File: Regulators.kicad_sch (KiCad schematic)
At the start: 20 parts, among them IC1 LT8631IFE#PBF, J10 1935161

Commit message: progress
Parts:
- C53: renamed from C1; footprint CAPAE1360X1450N -> SamacSys_Parts:CAPAE1360X1450N
- renumbered C13 to C54, C16 to C55, C18 to C56, C20 to C57, C21 to C58, C23 to C59, C17 to C60, D22 to D24, D3 to D25, IC1 to IC2, J10 to J18, R91 to R90, R108 to R91, R44 to R92, R45 to R93, R46 to R94, R47 to R95, R48 to R96
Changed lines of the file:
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@@
 		(dnp no)
 		(fields_autoplaced yes)
-		(property "Reference" "C13"
+		(property "Reference" "C54"
 			(at 139.7 44.4499 0)
 			(show_name no)
@@
 			(project "kiln"
 				(path "/e9c1836b-d16f-494a-819b-41549a786e18/415569b5-e71f-44a8-96ab-1860fbe1fd72"
-					(reference "C15")
+					(reference "C62")
 					(unit 1)
 				)
 				(path "/e9c1836b-d16f-494a-819b-41549a786e18/79a7153e-7b60-438c-928b-888b0e0879ef"
-					(reference "C13")
+					(reference "C54")
 					(unit 1)
 				)
@@
 		(dnp no)
 		(fields_autoplaced yes)
-		(property "Reference" "R91"
+		(property "Reference" "R90"
 			(at 123.19 76.1999 0)
 			(show_name no)
@@
 			(project "kiln"
 				(path "/e9c1836b-d16f-494a-819b-41549a786e18/415569b5-e71f-44a8-96ab-1860fbe1fd72"
-					(reference "R107")
+					(reference "R97")
 					(unit 1)
 				)
 				(path "/e9c1836b-d16f-494a-819b-41549a786e18/79a7153e-7b60-438c-928b-888b0e0879ef"
-					(reference "R91")
+					(reference "R90")
 					(unit 1)
 				)
@@
 		(dnp no)
 		(fields_autoplaced yes)
-		(property "Reference" "R47"
+		(property "Reference" "R95"
 			(at 236.22 81.2799 0)
 			(show_name no)
@@
 			(project "kiln"
 				(path "/e9c1836b-d16f-494a-819b-41549a786e18/415569b5-e71f-44a8-96ab-1860fbe1fd72"
-					(reference "R87")
+					(reference "R102")
 					(unit 1)
 				)
 				(path "/e9c1836b-d16f-494a-819b-41549a786e18/79a7153e-7b60-438c-928b-888b0e0879ef"
-					(reference "R47")
+					(reference "R95")
 					(unit 1)
 				)
@@
 		(in_pos_files yes)
 		(dnp no)
-		(property "Reference" "C18"
+		(property "Reference" "C56"
 			(at 202.438 85.344 0)
 			(show_name no)
@@
 			(project "kiln"
 				(path "/e9c1836b-d16f-494a-819b-41549a786e18/415569b5-e71f-44a8-96ab-1860fbe1fd72"
-					(reference "C45")
+					(reference "C64")
 					(unit 1)
 				)
 				(path "/e9c1836b-d16f-494a-819b-41549a786e18/79a7153e-7b60-438c-928b-888b0e0879ef"
-					(reference "C18")
+					(reference "C56")
 					(unit 1)
 				)
@@
 		(dnp no)
 		(fields_autoplaced yes)
-		(property "Reference" "C17"
+		(property "Reference" "C60"
 			(at 266.7 85.0899 0)
 			(show_name no)
@@
 			(project "kiln"
 				(path "/e9c1836b-d16f-494a-819b-41549a786e18/415569b5-e71f-44a8-96ab-1860fbe1fd72"
-					(reference "C49")
+					(reference "C68")
 					(unit 1)
 				)
 				(path "/e9c1836b-d16f-494a-819b-41549a786e18/79a7153e-7b60-438c-928b-888b0e0879ef"
-					(reference "C17")
+					(reference "C60")
 					(unit 1)
 				)
@@
 		(dnp no)
 		(fields_autoplaced yes)
-		(property "Reference" "C21"
+		(property "Reference" "C58"
 			(at 224.79 80.0099 0)
 			(show_name no)
@@
 			(project "kiln"
 				(path "/e9c1836b-d16f-494a-819b-41549a786e18/415569b5-e71f-44a8-96ab-1860fbe1fd72"
-					(reference "C47")
+					(reference "C66")
 					(unit 1)
 				)
 				(path "/e9c1836b-d16f-494a-819b-41549a786e18/79a7153e-7b60-438c-928b-888b0e0879ef"
-					(reference "C21")
+					(reference "C58")
 					(unit 1)
 				)
@@
 		(dnp no)
 		(fields_autoplaced yes)
-		(property "Reference" "D3"
+		(property "Reference" "D25"
 			(at 124.46 96.8374 90)
 			(show_name no)
@@
 			(project "kiln"
 				(path "/e9c1836b-d16f-494a-819b-41549a786e18/415569b5-e71f-44a8-96ab-1860fbe1fd72"
-					(reference "D4")
+					(reference "D27")
 					(unit 1)
 				)
 				(path "/e9c1836b-d16f-494a-819b-41549a786e18/79a7153e-7b60-438c-928b-888b0e0879ef"
-					(reference "D3")
+					(reference "D25")
 					(unit 1)
 				)
@@
 			(project "kiln"
 				(path "/e9c1836b-d16f-494a-819b-41549a786e18/415569b5-e71f-44a8-96ab-1860fbe1fd72"
-					(reference "L5")
+					(reference "L3")
 					(unit 1)
 				)
@@
 		(dnp no)
 		(fields_autoplaced yes)
-		(property "Reference" "IC1"
+		(property "Reference" "IC2"
 			(at 184.15 48.26 0)
 			(show_name no)
@@
 			(project "kiln"
 				(path "/e9c1836b-d16f-494a-819b-41549a786e18/415569b5-e71f-44a8-96ab-1860fbe1fd72"
+					(reference "IC3")
+					(unit 1)
+				)
+				(path "/e9c1836b-d16f-494a-819b-41549a786e18/79a7153e-7b60-438c-928b-888b0e0879ef"
 					(reference "IC2")
-					(unit 1)
-				)
-				(path "/e9c1836b-d16f-494a-819b-41549a786e18/79a7153e-7b60-438c-928b-888b0e0879ef"
-					(reference "IC1")
 					(unit 1)
 				)
@@
 		(dnp no)
 		(fields_autoplaced yes)
-		(property "Reference" "R108"
+		(property "Reference" "R91"
 			(at 123.19 85.0899 0)
 			(show_name no)
@@
 			(project "kiln"
 				(path "/e9c1836b-d16f-494a-819b-41549a786e18/415569b5-e71f-44a8-96ab-1860fbe1fd72"
-					(reference "R109")
+					(reference "R98")
 					(unit 1)
 				)
 				(path "/e9c1836b-d16f-494a-819b-41549a786e18/79a7153e-7b60-438c-928b-888b0e0879ef"
-					(reference "R108")
+					(reference "R91")
 					(unit 1)
 				)
@@
 		(dnp no)
 		(fields_autoplaced yes)
-		(property "Reference" "C16"
+		(property "Reference" "C55"
 			(at 163.83 88.8999 0)
 			(show_name no)
@@
 			(project "kiln"
 				(path "/e9c1836b-d16f-494a-819b-41549a786e18/415569b5-e71f-44a8-96ab-1860fbe1fd72"
-					(reference "C19")
+					(reference "C63")
 					(unit 1)
 				)
 				(path "/e9c1836b-d16f-494a-819b-41549a786e18/79a7153e-7b60-438c-928b-888b0e0879ef"
-					(reference "C16")
+					(reference "C55")
 					(unit 1)
 				)
@@
 		(dnp no)
 		(fields_autoplaced yes)
-		(property "Reference" "C1"
+		(property "Reference" "C53"
 			(at 124.46 45.7199 90)
 			(show_name no)
@@
 			)
 		)
-		(property "Footprint" "CAPAE1360X1450N"
+		(property "Footprint" "SamacSys_Parts:CAPAE1360X1450N"
 			(at 121.92 49.53 0)
 			(hide yes)
@@
 			(project "kiln"
 				(path "/e9c1836b-d16f-494a-819b-41549a786e18/415569b5-e71f-44a8-96ab-1860fbe1fd72"
-					(reference "C2")
+					(reference "C61")
 					(unit 1)
 				)
 				(path "/e9c1836b-d16f-494a-819b-41549a786e18/79a7153e-7b60-438c-928b-888b0e0879ef"
-					(reference "C1")
+					(reference "C53")
 					(unit 1)
 				)
@@
 		(dnp no)
 		(fields_autoplaced yes)
-		(property "Reference" "R46"
+		(property "Reference" "R94"
 			(at 152.4 83.8199 0)
 			(show_name no)
@@
 			(project "kiln"
 				(path "/e9c1836b-d16f-494a-819b-41549a786e18/415569b5-e71f-44a8-96ab-1860fbe1fd72"
-					(reference "R81")
+					(reference "R101")
 					(unit 1)
 				)
 				(path "/e9c1836b-d16f-494a-819b-41549a786e18/79a7153e-7b60-438c-928b-888b0e0879ef"
-					(reference "R46")
+					(reference "R94")
 					(unit 1)
 				)
@@
 		(in_pos_files yes)
 		(dnp no)
-		(property "Reference" "J10"
+		(property "Reference" "J18"
 			(at 90.17 35.56 0)
 			(show_name no)
@@
 				)
 				(path "/e9c1836b-d16f-494a-819b-41549a786e18/79a7153e-7b60-438c-928b-888b0e0879ef"
-					(reference "J10")
+					(reference "J18")
 					(unit 1)
 				)
@@
 		(dnp no)
 		(fields_autoplaced yes)
-		(property "Reference" "R45"
+		(property "Reference" "R93"
 			(at 149.86 54.6099 0)
 			(show_name no)
@@
 			(project "kiln"
 				(path "/e9c1836b-d16f-494a-819b-41549a786e18/415569b5-e71f-44a8-96ab-1860fbe1fd72"
-					(reference "R80")
+					(reference "R100")
 					(unit 1)
 				)
 				(path "/e9c1836b-d16f-494a-819b-41549a786e18/79a7153e-7b60-438c-928b-888b0e0879ef"
-					(reference "R45")
+					(reference "R93")
 					(unit 1)
 				)
@@
 		(in_pos_files yes)
 		(dnp no)
-		(property "Reference" "C23"
+		(property "Reference" "C59"
 			(at 246.634 86.868 90)
 			(show_name no)
@@
 			(project "kiln"
 				(path "/e9c1836b-d16f-494a-819b-41549a786e18/415569b5-e71f-44a8-96ab-1860fbe1fd72"
-					(reference "C48")
+					(reference "C67")
 					(unit 1)
 				)
 				(path "/e9c1836b-d16f-494a-819b-41549a786e18/79a7153e-7b60-438c-928b-888b0e0879ef"
-					(reference "C23")
+					(reference "C59")
 					(unit 1)
 				)
@@
 		(dnp no)
 		(fields_autoplaced yes)
-		(property "Reference" "R48"
+		(property "Reference" "R96"
 			(at 236.22 91.4399 0)
 			(show_name no)
@@
 			(project "kiln"
 				(path "/e9c1836b-d16f-494a-819b-41549a786e18/415569b5-e71f-44a8-96ab-1860fbe1fd72"
-					(reference "R88")
+					(reference "R103")
 					(unit 1)
 				)
 				(path "/e9c1836b-d16f-494a-819b-41549a786e18/79a7153e-7b60-438c-928b-888b0e0879ef"
-					(reference "R48")
+					(reference "R96")
 					(unit 1)
 				)
@@
 		(in_pos_files yes)
 		(dnp no)
-		(property "Reference" "D22"
+		(property "Reference" "D24"
 			(at 107.696 44.958 90)
 			(show_name no)
@@
 			(project "kiln"
 				(path "/e9c1836b-d16f-494a-819b-41549a786e18/415569b5-e71f-44a8-96ab-1860fbe1fd72"
-					(reference "D35")
+					(reference "D26")
 					(unit 1)
 				)
 				(path "/e9c1836b-d16f-494a-819b-41549a786e18/79a7153e-7b60-438c-928b-888b0e0879ef"
-					(reference "D22")
+					(reference "D24")
 					(unit 1)
 				)
@@
 		(dnp no)
 		(fields_autoplaced yes)
-		(property "Reference" "R44"
+		(property "Reference" "R92"
 			(at 149.86 44.4499 0)
 			(show_name no)
@@
 			(project "kiln"
 				(path "/e9c1836b-d16f-494a-819b-41549a786e18/415569b5-e71f-44a8-96ab-1860fbe1fd72"
-					(reference "R79")
+					(reference "R99")
 					(unit 1)
 				)
 				(path "/e9c1836b-d16f-494a-819b-41549a786e18/79a7153e-7b60-438c-928b-888b0e0879ef"
-					(reference "R44")
+					(reference "R92")
 					(unit 1)
 				)
@@
 		(dnp no)
 		(fields_autoplaced yes)
-		(property "Reference" "C20"
+		(property "Reference" "C57"
 			(at 220.98 54.6099 0)
 			(show_name no)
@@
 			(project "kiln"
 				(path "/e9c1836b-d16f-494a-819b-41549a786e18/415569b5-e71f-44a8-96ab-1860fbe1fd72"
-					(reference "C46")
+					(reference "C65")
 					(unit 1)
 				)
 				(path "/e9c1836b-d16f-494a-819b-41549a786e18/79a7153e-7b60-438c-928b-888b0e0879ef"
-					(reference "C20")
-					(unit 1)
-				)
+					(reference "C57")
+					(unit 1)
+				)

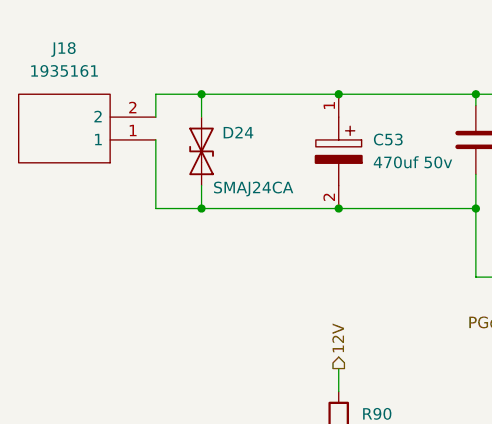
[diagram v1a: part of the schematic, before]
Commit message: why does c12 have a diffrent footprint from c67 and c56
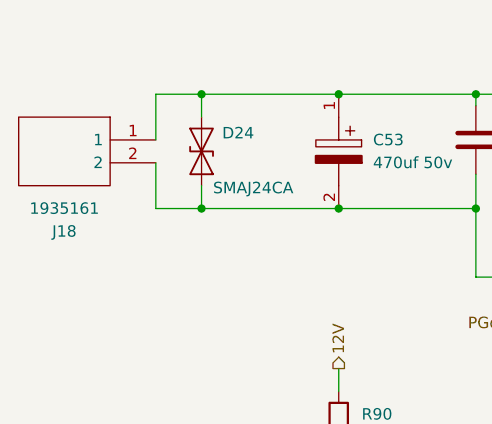
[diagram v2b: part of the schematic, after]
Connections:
- net 12V: now also J18.1; no longer J18.2
- net PwrGnd: now also J18.2; no longer J18.1
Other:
- moved on the sheet: J18
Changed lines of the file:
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@@
+	)
+	(junction
+		(at 243.84 97.79)
+		(diameter 0)
+		(color 0 0 0 0)
+	)
+	(junction
+		(at 233.68 76.2)
+		(diameter 0)
+		(color 0 0 0 0)
+	)
+	(junction
+		(at 144.78 40.64)
+		(diameter 0)
+		(color 0 0 0 0)
+	)
+	(junction
+		(at 147.32 40.64)
+		(diameter 0)
+		(color 0 0 0 0)
+	)
+	(junction
+		(at 120.65 40.64)
+		(diameter 0)
+		(color 0 0 0 0)
+	)
+	(junction
+		(at 250.19 97.79)
+		(diameter 0)
+		(color 0 0 0 0)
+	)
+	(junction
+		(at 233.68 97.79)
+		(diameter 0)
+		(color 0 0 0 0)
+	)
+	(junction
+		(at 147.32 60.96)
+		(diameter 0)
+		(color 0 0 0 0)
+	)
+	(junction
+		(at 120.65 53.34)
+		(diameter 0)
+		(color 0 0 0 0)
+	)
+	(junction
+		(at 105.41 53.34)
+		(diameter 0)
+		(color 0 0 0 0)
+	)
+	(junction
+		(at 160.02 97.79)
+		(diameter 0)
+		(color 0 0 0 0)
+	)
+	(junction
+		(at 135.89 53.34)
+		(diameter 0)
+		(color 0 0 0 0)
+	)
+	(junction
+		(at 147.32 76.2)
+		(diameter 0)
+		(color 0 0 0 0)
+	)
+	(junction
+		(at 250.19 76.2)
+		(diameter 0)
+		(color 0 0 0 0)
+	)
+	(junction
+		(at 220.98 87.63)
+		(diameter 0)
+		(color 0 0 0 0)
+	)
+	(junction
+		(at 233.68 87.63)
+		(diameter 0)
+		(color 0 0 0 0)
+	)
+	(junction
+		(at 213.36 97.79)
+		(diameter 0)
+		(color 0 0 0 0)
+	)
+	(junction
+		(at 135.89 40.64)
+		(diameter 0)
+		(color 0 0 0 0)
 	)
 	(junction
@@
 	)
 	(junction
-		(at 243.84 97.79)
-		(diameter 0)
-		(color 0 0 0 0)
-	)
-	(junction
-		(at 233.68 76.2)
-		(diameter 0)
-		(color 0 0 0 0)
-	)
-	(junction
-		(at 144.78 40.64)
-		(diameter 0)
-		(color 0 0 0 0)
-	)
-	(junction
-		(at 147.32 40.64)
-		(diameter 0)
-		(color 0 0 0 0)
-	)
-	(junction
-		(at 120.65 40.64)
-		(diameter 0)
-		(color 0 0 0 0)
-	)
-	(junction
-		(at 250.19 97.79)
-		(diameter 0)
-		(color 0 0 0 0)
-	)
-	(junction
-		(at 233.68 97.79)
-		(diameter 0)
-		(color 0 0 0 0)
-	)
-	(junction
-		(at 147.32 60.96)
-		(diameter 0)
-		(color 0 0 0 0)
-	)
-	(junction
-		(at 120.65 53.34)
-		(diameter 0)
-		(color 0 0 0 0)
-	)
-	(junction
-		(at 105.41 53.34)
-		(diameter 0)
-		(color 0 0 0 0)
-	)
-	(junction
-		(at 160.02 97.79)
-		(diameter 0)
-		(color 0 0 0 0)
-	)
-	(junction
-		(at 135.89 53.34)
-		(diameter 0)
-		(color 0 0 0 0)
-	)
-	(junction
-		(at 147.32 76.2)
-		(diameter 0)
-		(color 0 0 0 0)
-	)
-	(junction
-		(at 250.19 76.2)
-		(diameter 0)
-		(color 0 0 0 0)
-	)
-	(junction
-		(at 220.98 87.63)
-		(diameter 0)
-		(color 0 0 0 0)
-	)
-	(junction
-		(at 233.68 87.63)
-		(diameter 0)
-		(color 0 0 0 0)
-	)
-	(junction
-		(at 213.36 97.79)
-		(diameter 0)
-		(color 0 0 0 0)
-	)
-	(junction
-		(at 135.89 40.64)
-		(diameter 0)
-		(color 0 0 0 0)
-	)
-	(junction
 		(at 147.32 50.8)
 		(diameter 0)
@@
 	(wire
 		(pts
+			(xy 100.33 40.64) (xy 105.41 40.64)
+		)
+		(stroke
+			(width 0)
+			(type default)
+		)
+	)
+	(wire
+		(pts
 			(xy 207.01 83.82) (xy 207.01 66.04)
 		)
@@
 	(wire
 		(pts
-			(xy 100.33 40.64) (xy 105.41 40.64)
-		)
-		(stroke
-			(width 0)
-			(type default)
-		)
-	)
-	(wire
-		(pts
 			(xy 144.78 38.1) (xy 144.78 40.64)
 		)
@@
 	(wire
 		(pts
-			(xy 100.33 53.34) (xy 100.33 45.72)
-		)
-		(stroke
-			(width 0)
-			(type default)
-		)
-	)
-	(wire
-		(pts
 			(xy 204.47 60.96) (xy 217.17 60.96)
 		)
@@
 	(wire
 		(pts
+			(xy 100.33 45.72) (xy 100.33 40.64)
+		)
+		(stroke
+			(width 0)
+			(type default)
+		)
+	)
+	(wire
+		(pts
+			(xy 100.33 48.26) (xy 100.33 53.34)
+		)
+		(stroke
+			(width 0)
+			(type default)
+		)
+	)
+	(wire
+		(pts
 			(xy 207.01 91.44) (xy 207.01 97.79)
 		)
@@
 		(pts
 			(xy 233.68 71.12) (xy 204.47 71.12)
-		)
-		(stroke
-			(width 0)
-			(type default)
-		)
-	)
-	(wire
-		(pts
-			(xy 100.33 40.64) (xy 100.33 43.18)
 		)
 		(stroke
@@
 	(symbol
 		(lib_id "SamacSys_Parts:1935161")
-		(at 100.33 45.72 180)
+		(at 100.33 45.72 0)
+		(mirror y)
 		(unit 1)
 		(body_style 1)
@@
 		(dnp no)
 		(property "Reference" "J18"
-			(at 90.17 35.56 0)
+			(at 90.17 55.88 0)
 			(show_name no)
 			(do_not_autoplace no)
@@
 		)
 		(property "Value" "1935161"
-			(at 90.17 38.1 0)
+			(at 90.17 53.34 0)
 			(show_name no)
 			(do_not_autoplace no)
@@
 		)
 		(property "Footprint" "SamacSys_Parts:1935161"
-			(at 83.82 48.26 0)
+			(at 83.82 43.18 0)
 			(hide yes)
 			(show_name no)
@@
 		)
 		(property "Description_1" "Phoenix Contact COMBICON PT PCB Terminal Block, 2 Way/Pole, Screw Terminals, 26  14 AWG Through Hole, Nylon"
-			(at 83.82 43.18 0)
+			(at 83.82 48.26 0)
 			(hide yes)
 			(show_name no)
@@
 		)
 		(property "Height" "11.55"
-			(at 83.82 40.64 0)
+			(at 83.82 50.8 0)
 			(hide yes)
 			(show_name no)
@@
 		)
 		(property "Mouser Part Number" "651-1935161"
-			(at 83.82 38.1 0)
+			(at 83.82 53.34 0)
 			(hide yes)
 			(show_name no)
@@
 		)
 		(property "Mouser Price/Stock" "https://www.mouser.co.uk/ProductDetail/Phoenix-Contact/1935161?qs=W3wJikR1%252BS6eKzfFl8Rbew%3D%3D"
-			(at 83.82 35.56 0)
+			(at 83.82 55.88 0)
 			(hide yes)
 			(show_name no)
@@
 		)
 		(property "Manufacturer_Name" "Phoenix Contact"
-			(at 83.82 33.02 0)
+			(at 83.82 58.42 0)
 			(hide yes)
 			(show_name no)
@@
 		)
 		(property "Manufacturer_Part_Number" "1935161"
-			(at 83.82 30.48 0)
-			(hide yes)
-			(show_name no)
+			(at 83.82 60.96 0)
+			(hide yes)
+			(show_name no)

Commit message: progress
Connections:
- net 12V: now also J18.2; no longer J18.1
- net PwrGnd: now also J18.1; no longer J18.2
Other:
- moved on the sheet: J18

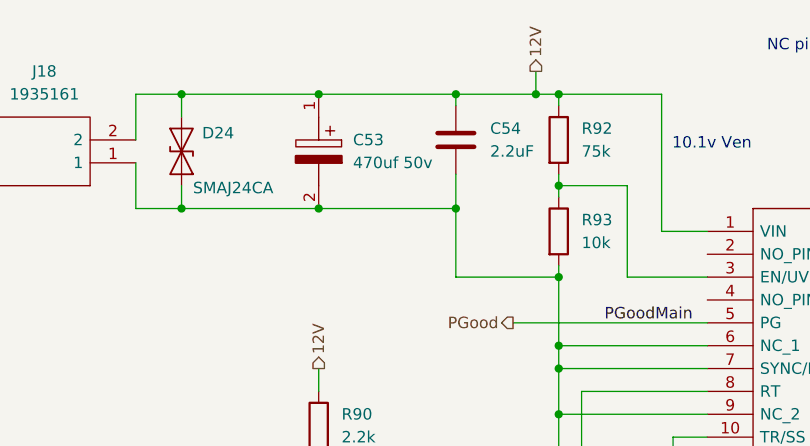
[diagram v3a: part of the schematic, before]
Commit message: add mouser sch tooling
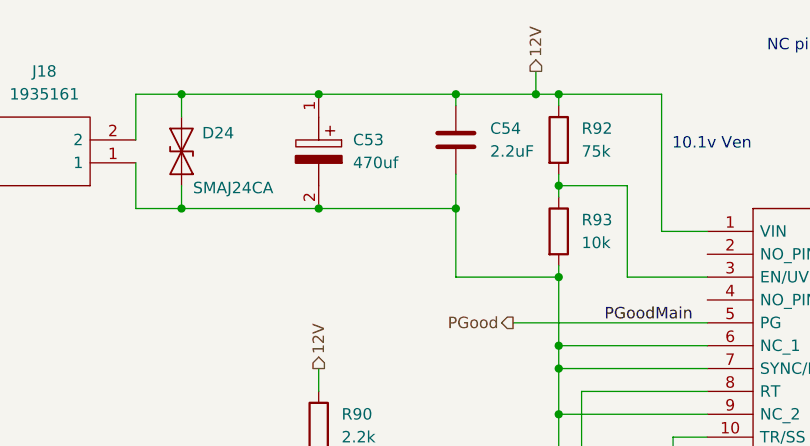
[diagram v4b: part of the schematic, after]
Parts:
- C53: value 470uf 50v -> 470uf
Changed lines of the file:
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@@
 			)
 		)
-		(property "Value" "470uf 50v"
+		(property "Value" "470uf"
 			(at 124.46 48.2599 90)
 			(show_name no)

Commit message: more tooling and updateing of the sch
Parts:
- C59: Mouser https://www.mouser.com/ProductDetail/Murata-Electronics/GRM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 -> https://www.mouser.com/en/ProductDetail/Samsung-Electro-Mec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
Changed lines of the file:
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@@
 			)
 		)
-		(property "Datasheet" "https://www.mouser.com/datasheet/2/281/1/GRM32EC81C476KE15_01A-1988154.pdf"
+		(property "Datasheet" "https://www.mouser.com/en/ProductDetail/Samsung-Electro-Mechanics/CL32A476KOJNNNE?qs=d72FGnIDsgQXYP%252BbBe7Sww%3D%3D"
 			(at 250.19 85.09 0)
 			(hide yes)
@@
 			)
 		)
-		(property "Mouser" "https://www.mouser.com/ProductDetail/Murata-Electronics/GRM32EC81C476KE15L?qs=eeBpzGFlv%252B%2F0ttt4zOip7g%3D%3D"
+		(property "Mouser" "https://www.mouser.com/en/ProductDetail/Samsung-Electro-Mechanics/CL32A476KOJNNNE?qs=d72FGnIDsgQXYP%252BbBe7Sww%3D%3D"
 			(at 250.19 85.09 90)
 			(hide yes)
@@
 			)
 		)
-		(property "Datasheet" "https://www.mouser.com/ProductDetail/Vishay/CRCW040247K5FKED?qs=sGAEpiMZZMtlubZbdhIBIPs%252BiE%2F4M15xDan5FFmucgw%3D"
+		(property "Datasheet" "https://www.mouser.com/en/ProductDetail/Vishay/CRCW0402154KFKED?qs=sGAEpiMZZMtlubZbdhIBICyxlhGRQNJfRCzUCssnsug%3D"
 			(at 233.68 92.71 0)
 			(hide yes)

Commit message: start adding seprate Thermocouple Board, fix some errors
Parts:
- C54, C56: Mouser Part Number Alt (none) -> https://www.mouser.com/en/ProductDetail/Samsung-Electro-Mec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; Mouser Part Number Alt 2 (none) -> https://www.mouser.com/en/ProductDetail/Murata-Electronics/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; Mouser Part Number Alt 3 (none) -> https://www.mouser.com/en/ProductDetail/Murata-Electronics/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; Mouser Part Number Alt 4 (none) -> https://www.mouser.com/en/ProductDetail/KEMET/C1206C225K5RA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
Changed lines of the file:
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@@
+			)
+		)
+		(property "Mouser Part Number Alt 4" "https://www.mouser.com/en/ProductDetail/KEMET/C1206C225K5RACAUTO7210?qs=%252BfJPIY6s7PlNVZKyV3SAGA%3D%3D"
+			(at 135.89 45.72 0)
+			(hide yes)
+			(show_name no)
+			(do_not_autoplace no)
+			(effects
+				(font
+					(size 1.27 1.27)
+				)
+			)
+		)
+		(property "Mouser Part Number Alt 3" "https://www.mouser.com/en/ProductDetail/Murata-Electronics/GCM31CR71H225KA55L?qs=aEuGZpxfbxXH69FledLqTA%3D%3D"
+			(at 135.89 45.72 0)
+			(hide yes)
+			(show_name no)
+			(do_not_autoplace no)
+			(effects
+				(font
+					(size 1.27 1.27)
+				)
+			)
+		)
+		(property "Mouser Part Number Alt 2" "https://www.mouser.com/en/ProductDetail/Murata-Electronics/GRT31CR71H225KE13L?qs=qkDYIeTQ%252BEkhrDhfEIGgfg%3D%3D"
+			(at 135.89 45.72 0)
+			(hide yes)
+			(show_name no)
+			(do_not_autoplace no)
+			(effects
+				(font
+					(size 1.27 1.27)
+				)
+			)
+		)
+		(property "Mouser Part Number Alt" "https://www.mouser.com/en/ProductDetail/Samsung-Electro-Mechanics/CL31B225KBHNFNE?qs=%252B6g0mu59x7Ixea%2FwRKCoRw%3D%3D"
+			(at 135.89 45.72 0)
+			(hide yes)
+			(show_name no)
+			(do_not_autoplace no)
+			(effects
+				(font
+					(size 1.27 1.27)
+				)
 			)
 		)
@@
 			(at 207.01 87.63 0)
 			(hide yes)
+			(show_name no)
+			(do_not_autoplace no)
+			(effects
+				(font
+					(size 1.27 1.27)
+				)
+			)
+		)
+		(property "Mouser Part Number Alt 4" "https://www.mouser.com/en/ProductDetail/KEMET/C1206C225K5RACAUTO7210?qs=%252BfJPIY6s7PlNVZKyV3SAGA%3D%3D"
+			(at 207.01 87.63 0)
+			(hide yes)
+			(show_name no)
+			(do_not_autoplace no)
+			(effects
+				(font
+					(size 1.27 1.27)
+				)
+			)
+		)
+		(property "Mouser Part Number Alt 3" "https://www.mouser.com/en/ProductDetail/Murata-Electronics/GCM31CR71H225KA55L?qs=aEuGZpxfbxXH69FledLqTA%3D%3D"
+			(at 207.01 87.63 0)
+			(hide yes)
+			(show_name no)
+			(do_not_autoplace no)
+			(effects
+				(font
+					(size 1.27 1.27)
+				)
+			)
+		)
+		(property "Mouser Part Number Alt 2" "https://www.mouser.com/en/ProductDetail/Murata-Electronics/GRT31CR71H225KE13L?qs=qkDYIeTQ%252BEkhrDhfEIGgfg%3D%3D"
+			(at 207.01 87.63 0)
+			(hide yes)
+			(show_name no)
+			(do_not_autoplace no)
+			(effects
+				(font
+					(size 1.27 1.27)
+				)
+			)
+		)
+		(property "Mouser Part Number Alt" "https://www.mouser.com/en/ProductDetail/Samsung-Electro-Mechanics/CL31B225KBHNFNE?qs=%252B6g0mu59x7Ixea%2FwRKCoRw%3D%3D"
+			(at 207.01 87.63 0)
+			(hide yes)
